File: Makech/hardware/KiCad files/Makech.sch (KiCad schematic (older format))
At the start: 44 parts, among them IC1 ULN2803, J1 SWD programmer, J2 USB_B_Micro, J3 ESP32-Exp, SW1 RST, SW2 SW_DPDT_x2, U1 ATSAMD21G18A-AU, U2 CONN_01X04, U3 AP2114_3.3v, X1 Screw_Terminal_1x02

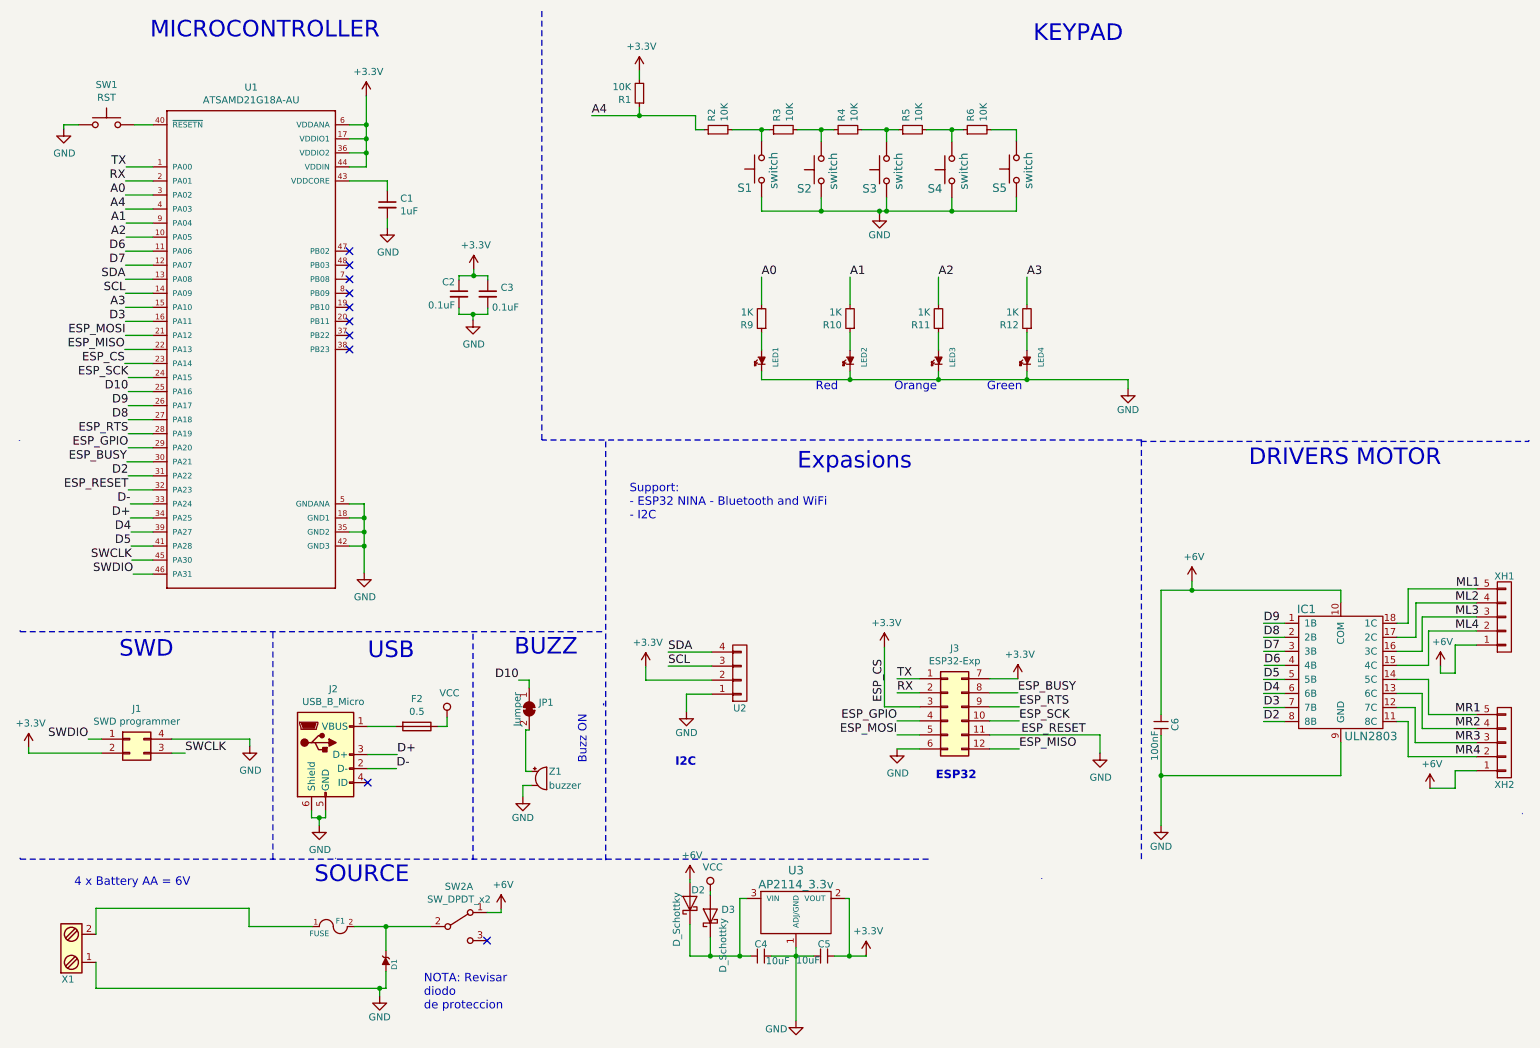
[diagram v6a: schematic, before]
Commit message: Change Fusible and add conector expansion
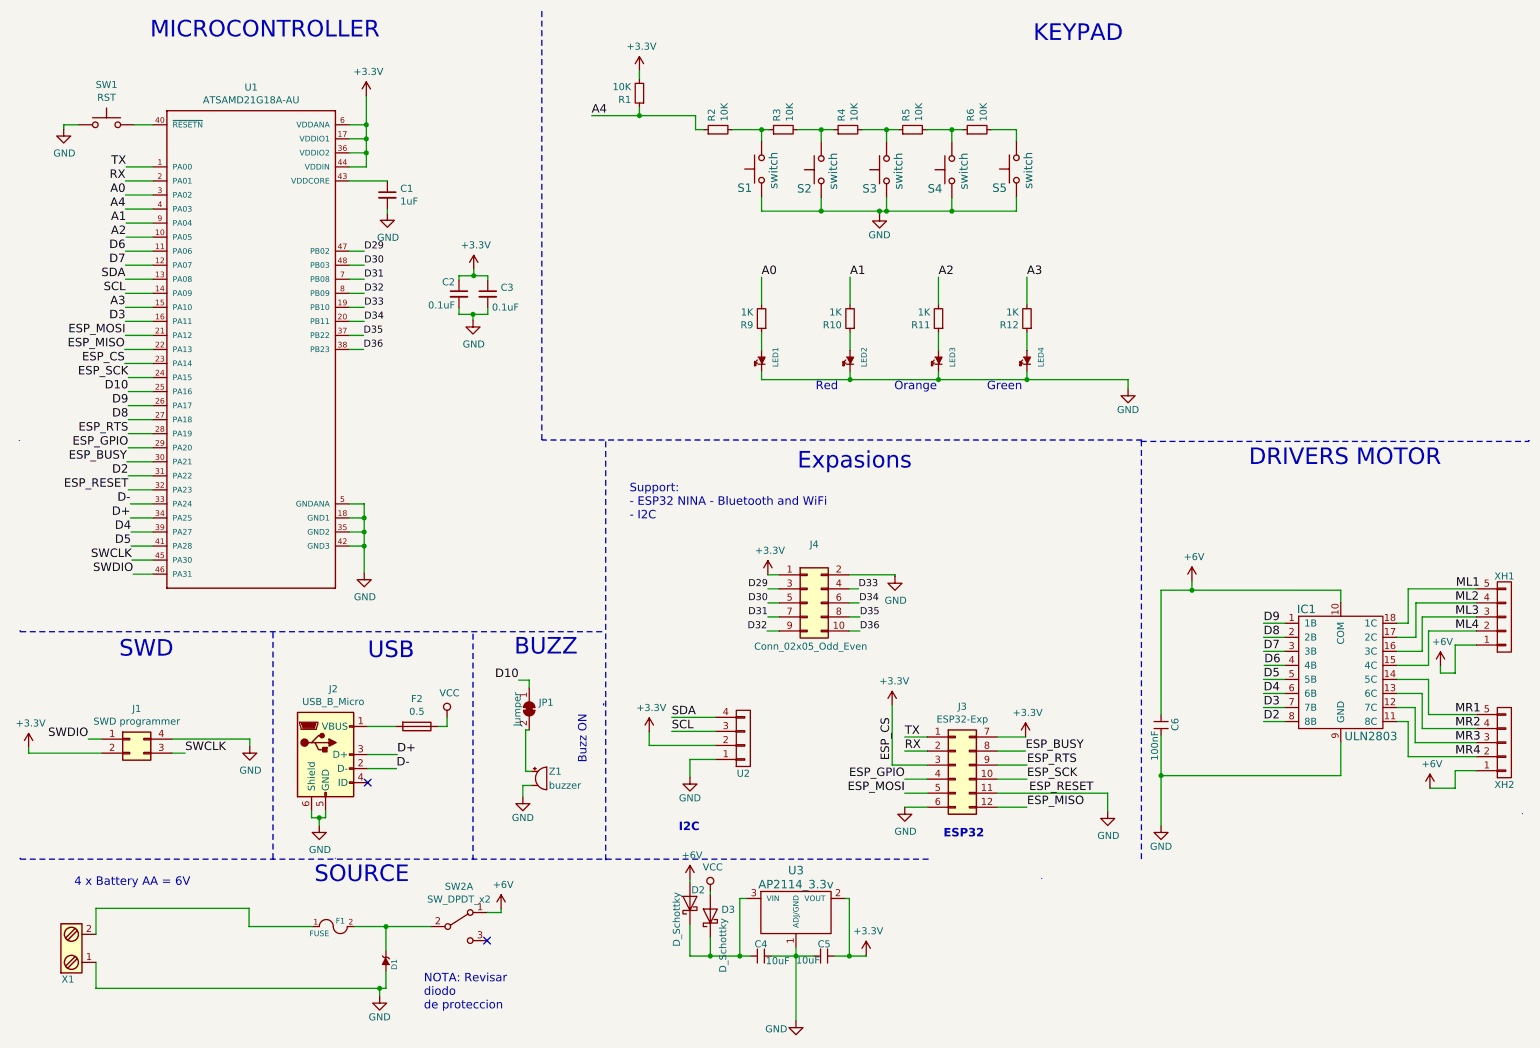
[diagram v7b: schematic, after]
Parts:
- added J4: Conn_02x05_Odd_Even, Pines:62001021121, symbol Connector_Generic:Conn_02x05_Odd_Even
- F1, F2: footprint Fuse:Fuse_0805_2012Metric -> Resistors_SMD:R_1812_HandSoldering
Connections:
- net +3V3: now also J4.1 (Pin_1)
- net GND: now also J4.2 (Pin_2)
- net D33: now reaches U1.19 (PB10)
- net D33: now also J4.4 (Pin_4)
- net D34: now reaches U1.20 (PB11)
- net D34: now also J4.6 (Pin_6)
- net D35: now reaches U1.37 (PB22)
- net D35: now also J4.8 (Pin_8)
- net D36: now reaches U1.38 (PB23)
- net D36: now also J4.10 (Pin_10)
- net D29: now reaches U1.47 (PB02)
- net D29: now also J4.3 (Pin_3)
- net D30: now reaches U1.48 (PB03)
- net D30: now also J4.5 (Pin_5)
- net D31: now reaches U1.7 (PB08)
- net D31: now also J4.7 (Pin_7)
- net D32: now reaches U1.8 (PB09)
- net D32: now also J4.9 (Pin_9)
- no-connect marks 10 -> 2
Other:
- moved on the sheet: C1, J3, U2

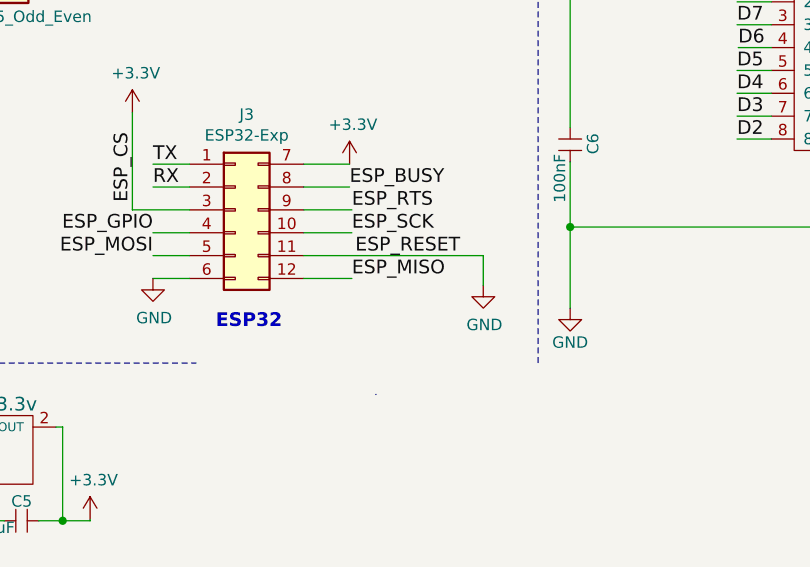
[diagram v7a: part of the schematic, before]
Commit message: Fix error NINA_RESET to GND
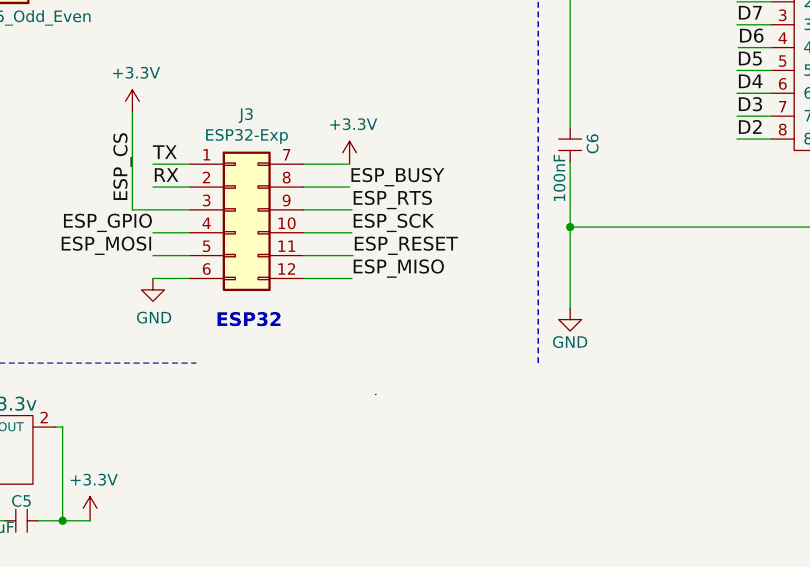
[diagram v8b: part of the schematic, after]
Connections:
- net GND: no longer J3.11 (Pin_11), U1.32 (PA23)
- new net ESP_RESET: J3.11 (Pin_11), U1.32 (PA23)
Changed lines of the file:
@@
 EESchema Schematic File Version 4
 LIBS:Makech-cache
-EELAYER 26 0
+EELAYER 29 0
 EELAYER END
 $Descr A4 11693 8268
@@
 	1    0    0    -1
 $EndComp
-Text Label 7660 6065 0    60   ~ 0
+Text Label 7650 6065 0    60   ~ 0
 ESP_RESET
 Text Label 4545 1240 0    60   ~ 0
@@
 	1    0    0    -1
 $EndComp
-Wire Wire Line
-	7435 6065 8220 6065
 Text Label 1245 3905 2    60   ~ 0
 ESP_RESET
@@
 Text Notes 2570 6715 0    118  ~ 0
 SOURCE
-$Comp
-L power:GND #PWR025
-U 1 1 5C99179E
-P 8220 6195
-F 0 "#PWR025" H 8220 5945 50  0001 C CNN
-F 1 "GND" H 8225 6022 50  0000 C CNN
-F 2 "" H 8220 6195 50  0001 C CNN
-F 3 "" H 8220 6195 50  0001 C CNN
-	1    8220 6195
-	1    0    0    -1
-$EndComp
-Wire Wire Line
-	8220 6065 8220 6195
 Wire Wire Line
 	6685 5440 6685 5865
@@
 Wire Wire Line
 	6380 4510 6705 4510
+Wire Wire Line
+	7435 6065 7650 6065
 $EndSCHEMATC
